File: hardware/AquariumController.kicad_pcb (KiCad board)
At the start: 2 copper layers, 70 x 100 mm, 51 parts, among them J1 Conn_01x07, J2 Conn_01x03, J3 Conn_01x04, J4 Conn_01x04, J5 Conn_01x02, J6 Conn_01x02, J7 Conn_01x02, J8 Conn_01x02, K1 SANYOU_SRD_Form_C, K2 SANYOU_SRD_Form_C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

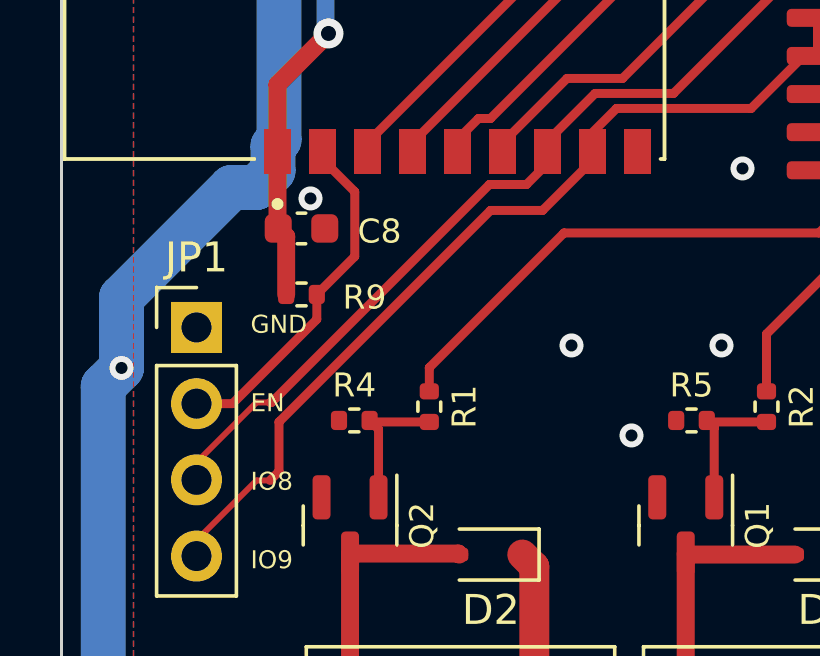
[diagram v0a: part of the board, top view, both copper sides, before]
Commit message: added C13 on EN
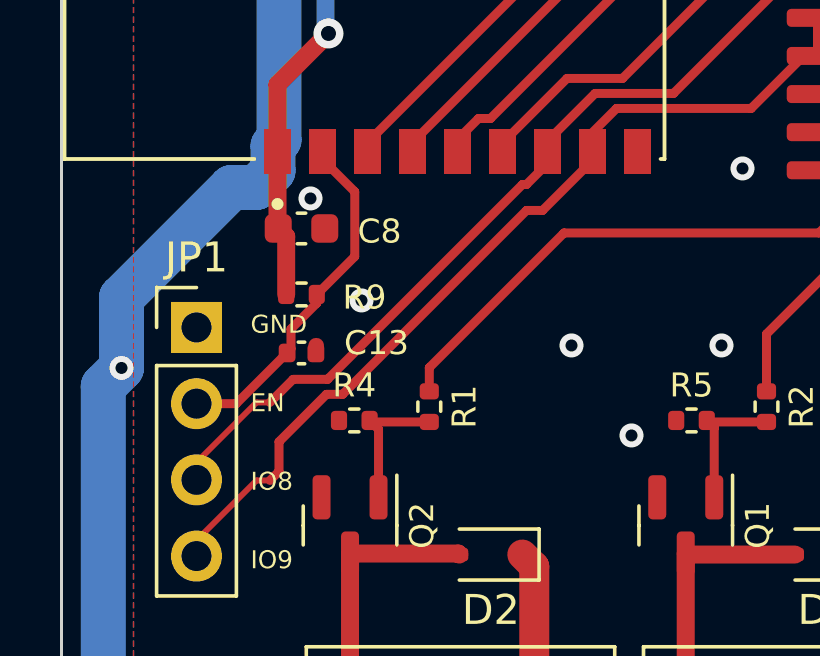
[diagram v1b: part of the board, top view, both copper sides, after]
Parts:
- added C13: 1uF, Capacitor_SMD:C_0402_1005Metric, F.Cu at (168.0, 100.2)
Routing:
- net GND: track 1.61 -> 1.63 mm, vias 27 -> 28

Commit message: NT1 move
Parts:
- moved NT1 0.60 mm to (166.7, 102.5)
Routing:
- net /IO8: track 3.41 -> 2.82 mm
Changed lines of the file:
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@@
   )
   (footprint "ProjectLibrary:NetTie-2_SMD_Pad0.2mm" (layer "F.Cu")
-    (at 166.7 101.9 180)
+    (at 166.7 102.5 180)
     (descr "Net tie, 2 pin, 0.5mm square SMD pads")
     (tags "net tie")
@@
   (segment (start 177.7 93.835) (end 176.035 95.5) (width 0.3) (layer "F.Cu") (net 11))
   (segment (start 180.4 91.6) (end 184.19 87.81) (width 0.3) (layer "F.Cu") (net 12))
-  (segment (start 167.72 101.13) (end 166.95 101.9) (width 0.3) (layer "F.Cu") (net 12))
-  (segment (start 168.87 101.13) (end 167.72 101.13) (width 0.3) (layer "F.Cu") (net 12))
+  (segment (start 176.2 93.535) (end 176.2 93.935) (width 0.3) (layer "F.Cu") (net 12))
+  (segment (start 176.2 93.935) (end 175.5 94.635) (width 0.3) (layer "F.Cu") (net 12))
+  (segment (start 175.365 94.635) (end 169.31 100.69) (width 0.3) (layer "F.Cu") (net 12))
+  (segment (start 168.37 101.13) (end 167 102.5) (width 0.3) (layer "F.Cu") (net 12))
   (segment (start 175.5 94.635) (end 175.365 94.635) (width 0.3) (layer "F.Cu") (net 12))
+  (segment (start 167 102.5) (end 166.95 102.5) (width 0.3) (layer "F.Cu") (net 12))
   (segment (start 177.785 91.6) (end 180.4 91.6) (width 0.3) (layer "F.Cu") (net 12))
-  (segment (start 176.2 93.535) (end 176.2 93.935) (width 0.3) (layer "F.Cu") (net 12))
   (segment (start 176.15 93.535) (end 176.15 93.235) (width 0.3) (layer "F.Cu") (net 12))
   (segment (start 184.19 87.81) (end 185.2 87.81) (width 0.3) (layer "F.Cu") (net 12))
   (segment (start 176.15 93.235) (end 177.785 91.6) (width 0.3) (layer "F.Cu") (net 12))
-  (segment (start 176.2 93.935) (end 175.5 94.635) (width 0.3) (layer "F.Cu") (net 12))
+  (segment (start 169.31 100.705807) (end 168.885807 101.13) (width 0.3) (layer "F.Cu") (net 12))
+  (segment (start 168.885807 101.13) (end 168.37 101.13) (width 0.3) (layer "F.Cu") (net 12))
   (segment (start 185.2 87.81) (end 185.2 86.54) (width 0.3) (layer "F.Cu") (net 12))
-  (segment (start 175.365 94.635) (end 168.87 101.13) (width 0.3) (layer "F.Cu") (net 12))
+  (segment (start 169.31 100.69) (end 169.31 100.705807) (width 0.3) (layer "F.Cu") (net 12))
   (segment (start 174.65 93.3) (end 176.85 91.1) (width 0.3) (layer "F.Cu") (net 13))
   (segment (start 184.53 85.27) (end 185.2 85.27) (width 0.3) (layer "F.Cu") (net 13))
@@
   (segment (start 164.5 107.02) (end 164.5 106.5) (width 0.2) (layer "F.Cu") (net 45))
   (segment (start 164.5 106.5) (end 166.5 104.5) (width 0.2) (layer "F.Cu") (net 45))
-  (segment (start 164.5 103.9) (end 166.5 101.9) (width 0.2) (layer "F.Cu") (net 46))
-  (segment (start 164.5 104.48) (end 164.5 103.9) (width 0.2) (layer "F.Cu") (net 46))
+  (segment (start 166.48 102.5) (end 166.5 102.5) (width 0.2) (layer "F.Cu") (net 46))
+  (segment (start 164.5 104.48) (end 166.48 102.5) (width 0.2) (layer "F.Cu") (net 46))
   (segment (start 213.5375 48.1875) (end 218.1 52.75) (width 2.5) (layer "B.Cu") (net 47))
   (segment (start 218.9 28.55) (end 217.895 29.555) (width 2.5) (layer "B.Cu") (net 47))

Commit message: 7.0.1-> 7.0.2, varistor update from library, temporary disable SPICE model issue violation
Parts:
- moved C8 0.20 mm to (168.0, 96.3)
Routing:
- net GND: vias 28 -> 32
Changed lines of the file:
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@@
   (net 45 "/IO9")
   (net 46 "/IO8")
-  (net 47 "Net-(#FLG04-pwr)")
+  (net 47 "Net-(PS1-AC{slash}L)")
   (net 48 "/IO2")
   (footprint "Capacitor_SMD:C_0603_1608Metric" (layer "F.Cu")
@@
       (stroke (width 0.1) (type solid)) (layer "F.Fab"))
     (pad "1" thru_hole rect (at 0 0 180) (size 2.3 2) (drill 1) (layers "*.Cu" "*.Mask" "B.Adhes")
-      (net 47 "Net-(#FLG04-pwr)") (pinfunction "AC/L") (pintype "power_in"))
+      (net 47 "Net-(PS1-AC{slash}L)") (pinfunction "AC/L") (pintype "power_in"))
     (pad "2" thru_hole circle (at 0 7.8 180) (size 2.3 2.3) (drill 1) (layers "*.Cu" "*.Mask")
       (net 41 "AL{slash}N") (pinfunction "AC/N") (pintype "power_in"))
@@
     (property "Sheetfile" "AquariumController.kicad_sch")
     (property "Sheetname" "")
+    (property "exclude_from_bom" "")
     (property "ki_description" "Jumper, 2-pole, open")
     (property "ki_keywords" "Jumper SPST")
-    (attr through_hole)
+    (attr through_hole exclude_from_bom)
     (fp_text reference "JP1" (at 0 -2.33) (layer "F.SilkS")
         (effects (font (size 1 1) (thickness 0.15)))
@@
     (property "ki_keywords" "cap capacitor")
     (attr smd)
-    (fp_text reference "C4" (at 0 -1.43) (layer "F.SilkS")
+    (fp_text reference "C4" (at 0 -1.3) (layer "F.SilkS")
         (effects (font (size 0.8 0.8) (thickness 0.15)))
     )
@@
       (net 41 "AL{slash}N") (pintype "passive"))
     (pad "2" thru_hole circle (at 7.5 1.4 270) (size 1.8 1.8) (drill 0.8) (layers "*.Cu" "*.Mask")
-      (net 47 "Net-(#FLG04-pwr)") (pintype "passive"))
+      (net 47 "Net-(PS1-AC{slash}L)") (pintype "passive"))
     (model "${KICAD6_3DMODEL_DIR}/Varistor.3dshapes/RV_Disc_D12mm_W3.9mm_P7.5mm.wrl"
       (offset (xyz 0 0 0))
@@
     (property "Sheetfile" "AquariumController.kicad_sch")
     (property "Sheetname" "")
+    (property "exclude_from_bom" "")
     (property "ki_description" "Generic connector, single row, 01x04, script generated (kicad-library-utils/schlib/autogen/connector/)")
     (property "ki_keywords" "connector")
-    (attr through_hole)
+    (attr through_hole exclude_from_bom)
     (fp_text reference "J3" (at 0 -2.33) (layer "F.SilkS")
         (effects (font (size 1 1) (thickness 0.15)))
@@
   )
   (footprint "Capacitor_SMD:C_0603_1608Metric" (layer "F.Cu")
-    (at 168 96.1 180)
+    (at 168 96.3 180)
     (descr "Capacitor SMD 0603 (1608 Metric), square (rectangular) end terminal, IPC_7351 nominal, (Body size source: IPC-SM-782 page 76, https://www.pcb-3d.com/wordpress/wp-content/uploads/ipc-sm-782a_amendment_1_and_2.pdf), generated with kicad-footprint-generator")
     (tags "capacitor")
@@
       (net 42 "AL{slash}L") (pintype "passive"))
     (pad "2" thru_hole circle (at 5.1 1.2 270) (size 2.01 2.01) (drill 1.01) (layers "*.Cu" "*.Mask")
-      (net 47 "Net-(#FLG04-pwr)") (pintype "passive"))
+      (net 47 "Net-(PS1-AC{slash}L)") (pintype "passive"))
     (model "${KICAD7_3DMODEL_DIR}/Fuse.3dshapes/Fuse_BelFuse_0ZRE_0ZRE0005FF_L8.3mm_W3.8mm.step"
       (offset (xyz 0 0 0))
@@
     (property "Sheetfile" "AquariumController.kicad_sch")
     (property "Sheetname" "")
+    (property "exclude_from_bom" "")
     (property "ki_description" "Generic connector, single row, 01x06, script generated (kicad-library-utils/schlib/autogen/connector/)")
     (property "ki_keywords" "connector")
-    (attr through_hole)
+    (attr through_hole exclude_from_bom)
     (fp_text reference "J4" (at 0 -2.33 90) (layer "F.SilkS")
         (effects (font (size 1 1) (thickness 0.15)))
@@
   (segment (start 168.48 100) (end 168.5 100) (width 0.5) (layer "F.Cu") (net 17))
   (via (at 182.7 77) (size 0.8) (drill 0.4) (layers "F.Cu" "B.Cu") (free) (net 17))
+  (via (at 190 53) (size 0.8) (drill 0.4) (layers "F.Cu" "B.Cu") (free) (net 17))
   (via (at 195 100) (size 0.8) (drill 0.4) (layers "F.Cu" "B.Cu") (free) (net 17))
+  (via (at 190 58) (size 0.8) (drill 0.4) (layers "F.Cu" "B.Cu") (free) (net 17))
   (via (at 181 54.7) (size 0.8) (drill 0.4) (layers "F.Cu" "B.Cu") (free) (net 17))
   (via (at 175.8 54.2) (size 0.8) (drill 0.4) (layers "F.Cu" "B.Cu") (free) (net 17))
@@
   (via (at 177 100) (size 0.8) (drill 0.4) (layers "F.Cu" "B.Cu") (free) (net 17))
   (via (at 177 42) (size 0.8) (drill 0.4) (layers "F.Cu" "B.Cu") (free) (net 17))
+  (via (at 182 47) (size 0.8) (drill 0.4) (layers "F.Cu" "B.Cu") (free) (net 17))
   (via (at 191.25 79.75) (size 0.8) (drill 0.4) (layers "F.Cu" "B.Cu") (free) (net 17))
   (via (at 196.25 55.75) (size 0.8) (drill 0.4) (layers "F.Cu" "B.Cu") (free) (net 17))
@@
   (via (at 182 100) (size 0.8) (drill 0.4) (layers "F.Cu" "B.Cu") (free) (net 17))
   (via (at 195 71) (size 0.8) (drill 0.4) (layers "F.Cu" "B.Cu") (free) (net 17))
+  (via (at 190 63) (size 0.8) (drill 0.4) (layers "F.Cu" "B.Cu") (free) (net 17))
   (via (at 190 89) (size 0.8) (drill 0.4) (layers "F.Cu" "B.Cu") (free) (net 17))
   (via (at 179 103) (size 0.8) (drill 0.4) (layers "F.Cu" "B.Cu") (free) (net 17))
@@
   (segment (start 167.2 73.59) (end 168.99 71.8) (width 0.2) (layer "F.Cu") (net 43))
   (segment (start 167.2 76.035) (end 167.2 73.59) (width 0.2) (layer "F.Cu") (net 43))
-  (segment (start 167.65 100.113604) (end 167.65 99.45) (width 0.3) (layer "F.Cu") (net 44))
-  (segment (start 168.7 93.8) (end 168.7 93.535) (width 0.3) (layer "F.Cu") (net 44))
+  (segment (start 168.51 98.3) (end 168.9 98.3) (width 0.3) (layer "F.Cu") (net 44))
+  (segment (start 169.65 97.55) (end 169.775 97.425) (width 0.3) (layer "F.Cu") (net 44))
   (segment (start 169.775 94.875) (end 168.7 93.8) (width 0.3) (layer "F.Cu") (net 44))
+  (segment (start 167.65 100.113604) (end 167.65 99.45) (width 0.3) (layer "F.Cu") (net 44))
+  (segment (start 168.9 98.3) (end 169.05 98.15) (width 0.3) (layer "F.Cu") (net 44))
+  (segment (start 169.05 98.15) (end 169.05 98.106497) (width 0.3) (layer "F.Cu") (net 44))
+  (segment (start 169.775 97.425) (end 169.775 94.875) (width 0.3) (layer "F.Cu") (net 44))
   (segment (start 165.823604 101.94) (end 167.65 100.113604) (width 0.3) (layer "F.Cu") (net 44))
-  (segment (start 168.51 98.3) (end 169.775 97.035) (width 0.3) (layer "F.Cu") (net 44))
+  (segment (start 168.7 93.8) (end 168.7 93.535) (width 0.3) (layer "F.Cu") (net 44))
   (segment (start 168.51 98.59) (end 168.51 98.3) (width 0.3) (layer "F.Cu") (net 44))
+  (segment (start 169.606497 97.55) (end 169.65 97.55) (width 0.3) (layer "F.Cu") (net 44))
   (segment (start 167.65 99.45) (end 168.51 98.59) (width 0.3) (layer "F.Cu") (net 44))
+  (segment (start 169.05 98.106497) (end 169.606497 97.55) (width 0.3) (layer "F.Cu") (net 44))
   (segment (start 164.5 101.94) (end 165.823604 101.94) (width 0.3) (layer "F.Cu") (net 44))
-  (segment (start 169.775 97.035) (end 169.775 94.875) (width 0.3) (layer "F.Cu") (net 44))
   (segment (start 164.5 107.02) (end 164.5 106.5) (width 0.2) (layer "F.Cu") (net 45))
   (segment (start 164.5 106.5) (end 166.5 104.5) (width 0.2) (layer "F.Cu") (net 45))
